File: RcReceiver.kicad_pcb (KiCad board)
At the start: 4 copper layers, 50 x 29.5 mm, 71 parts, among them J1 VBAT, J10 Servo3, J11 Servo4, J12 Servo5, J13 CAN, J14 Servo6, J15 Servo7, J16 Servo8, J17 GND for the Servo connectors, J2 SWD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

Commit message: Routing finished
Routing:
- net Net-(C24-Pad1): track 12.6 -> 11.7 mm
- net Net-(C25-Pad1): track 14.5 -> 13.9 mm
- net Net-(C23-Pad1): track 10.1 -> 9.56 mm
- net Net-(C27-Pad1): track 18.8 -> 18.3 mm
- net Net-(C21-Pad1): track 8.07 -> 7.56 mm

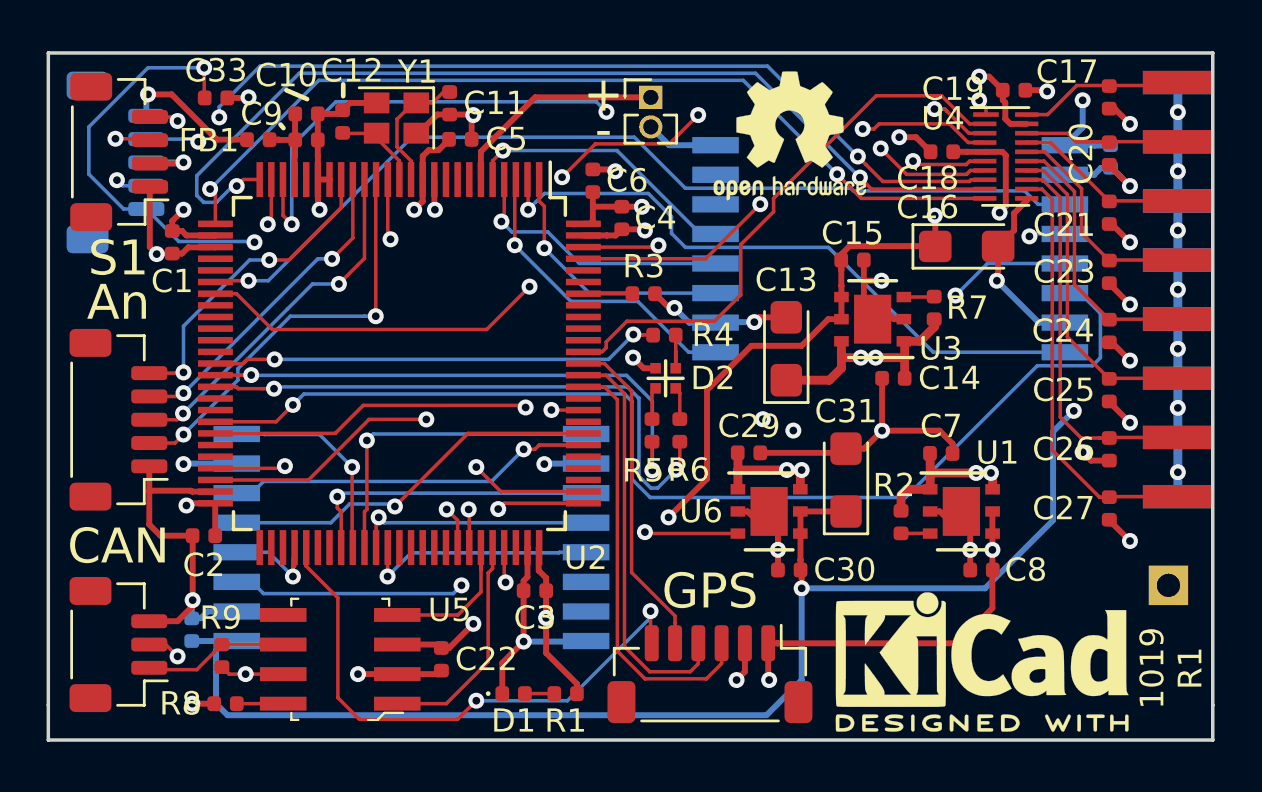
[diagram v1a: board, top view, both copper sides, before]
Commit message: Add fill zones
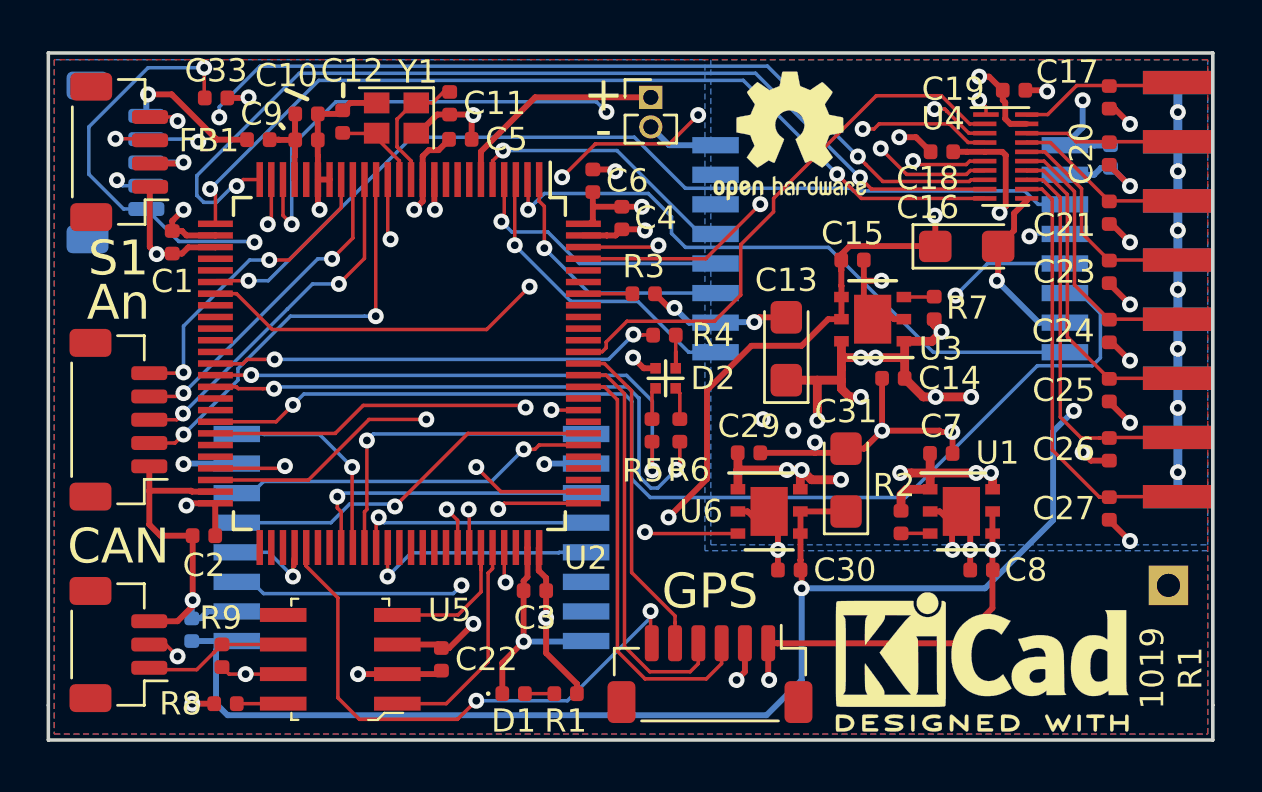
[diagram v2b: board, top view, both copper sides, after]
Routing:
- net IN: track 76.4 -> 93.7 mm, vias 13 -> 20
- net GND: track 289.3 -> 291.2 mm, vias 32 -> 35
- added copper zone on In2.Cu, net /VCCCPU
- added copper zone on B.Cu, net GND
- added copper zone on F.Cu, net GND
- added copper zone on In1.Cu, net GND
- added copper zone on B.Cu, net IN
- added copper zone on In2.Cu, net IN

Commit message: Change TBX0108 footprint
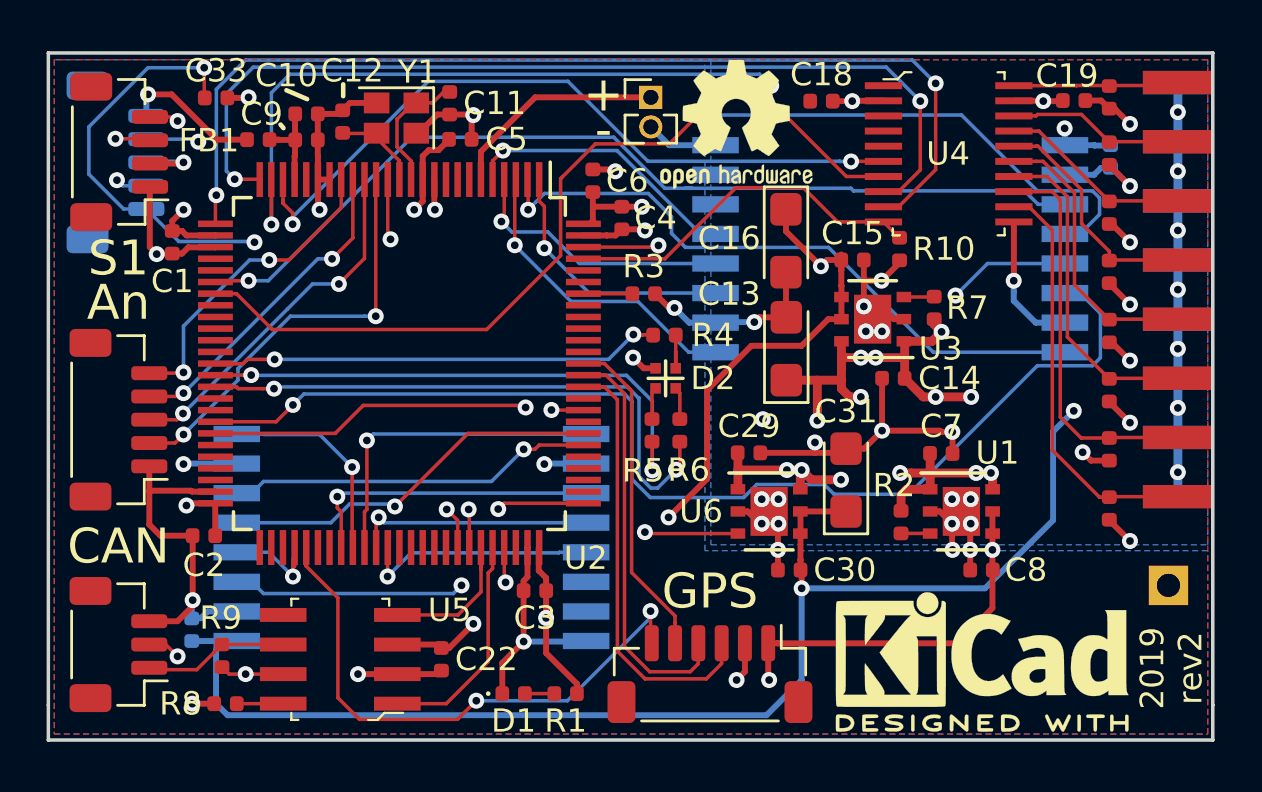
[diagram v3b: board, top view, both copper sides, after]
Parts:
- added R10: R, Resistor_SMD:R_0402_1005Metric, F.Cu at (172.6, 54.4)
- U4: value TXB0108DQSR -> TXB0108PWR; footprint Package_SON:USON-20_2x4mm_P0.4mm -> digikey-footprints:TSSOP-20_W4.4mm
- moved C16 7.76 mm to (167.7, 54.1), turned to 270 degrees
- moved C18 5.61 mm to (169.2, 48.1)
- moved C19 2.62 mm to (180.0, 48.0)
- moved U4 2.45 mm to (174.7, 50.3), turned to 270 degrees
- moved OSHLOGO 2.35 mm to (165.5, 49.1)
- renumbered C20 to wC20
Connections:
- U4 pad 10: /Connectors/PWM8 -> /PWMOE
- U4 pad 2: /PWM2 -> /VCCCPU
- U4 pad 3: /PWM3 -> /PWM2
- U4 pad 4: /PWM4 -> /PWM3
- U4 pad 5: /VCCCPU -> /PWM4
- U4 pad 6: /PWMOE -> /Connectors/PWM5
- U4 pad 7: /Connectors/PWM5 -> /Connectors/PWM6
- U4 pad 8: /Connectors/PWM6 -> /Connectors/PWM7
- U4 pad 9: /Connectors/PWM7 -> /Connectors/PWM8
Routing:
- net /PWM3: track 55.9 -> 0.00 mm, vias 2 -> 0
- net /PWM4: track 50.8 -> 0.00 mm, vias 2 -> 0
- net /PWM1: track 45.8 -> 0.00 mm, vias 3 -> 0
- net /PWM2: track 24.1 -> 0.05 mm
- net GND: track 291.2 -> 280.5 mm, vias 35 -> 44
- net /VCCCPU: track 160.5 -> 151.6 mm
- net /Connectors/PWM6: track 43.6 -> 36.4 mm, vias 3 -> 2
- net /Connectors/PWM5: track 37.3 -> 31.6 mm, vias 3 -> 2
- net /Connectors/PWM8: track 38.9 -> 44.2 mm
- net /PWMOE: track 19.1 -> 15.7 mm, vias 2 -> 0
- net /RF1MOSI: track 45.4 -> 48.4 mm, vias 4 -> 1
- net /RF modules/VCCRF: track 75.3 -> 72.6 mm
- net /Connectors/VCCOUT: track 46.4 -> 49.1 mm
- net /Connectors/PWM7: track 41.8 -> 40.7 mm
- net Net-(C20-Pad1): track 6.69 -> 7.62 mm
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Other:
- board text added: "2019 rev2"
- board text added: "RF module #1"
- board text removed: "1019 R1"
- board text removed: "RF Module #1"
